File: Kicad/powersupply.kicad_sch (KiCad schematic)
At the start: 19 parts, among them J801 Jack 2/6.3mm, Q801 BC546, Q802 BC556, U801 DC-DC Module, U802 MAX1615, U803 TLV1117 3.3V 1A

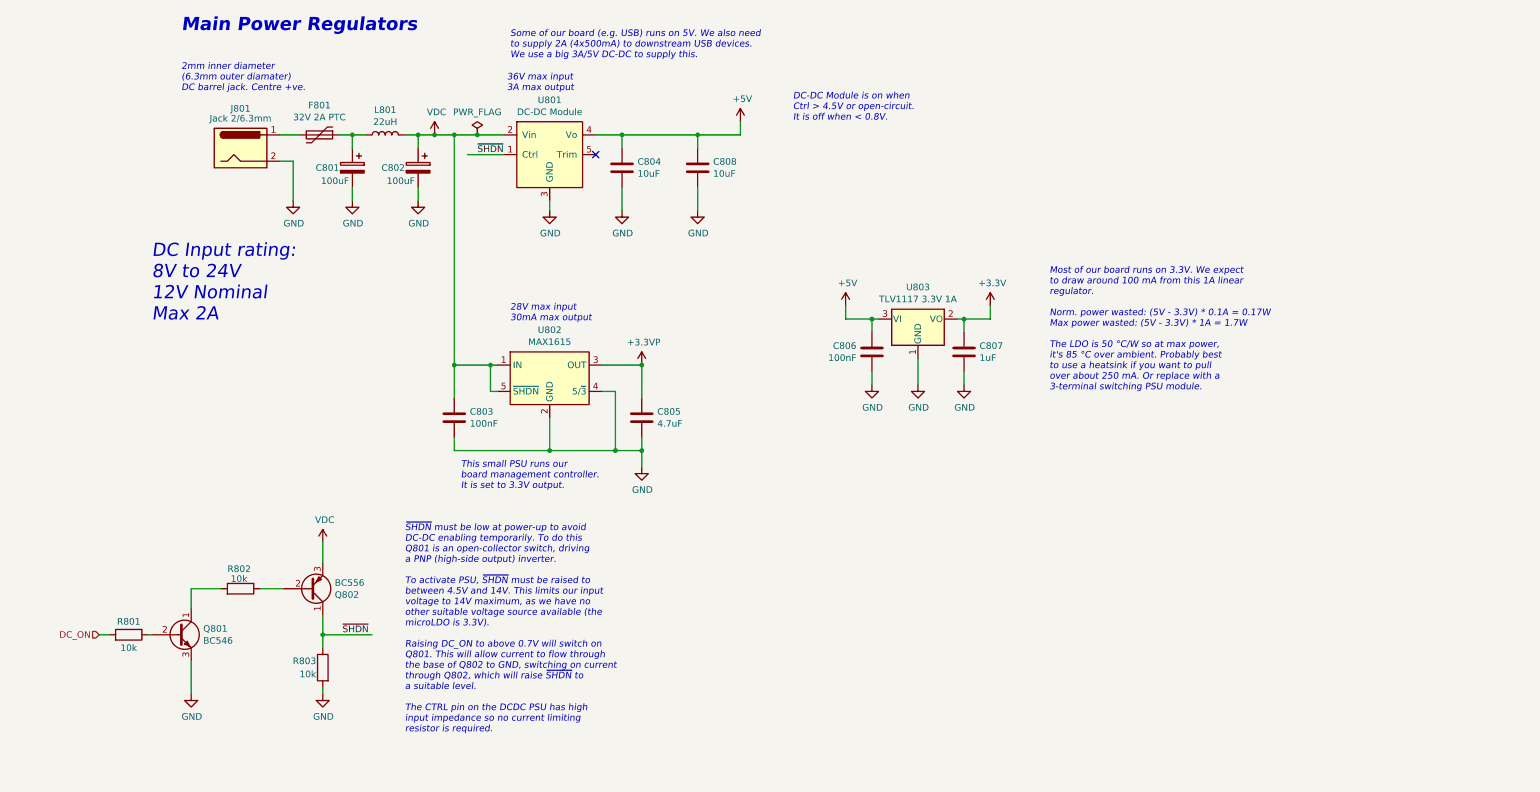
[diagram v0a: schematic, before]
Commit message: Retitle sheets and renumber parts.
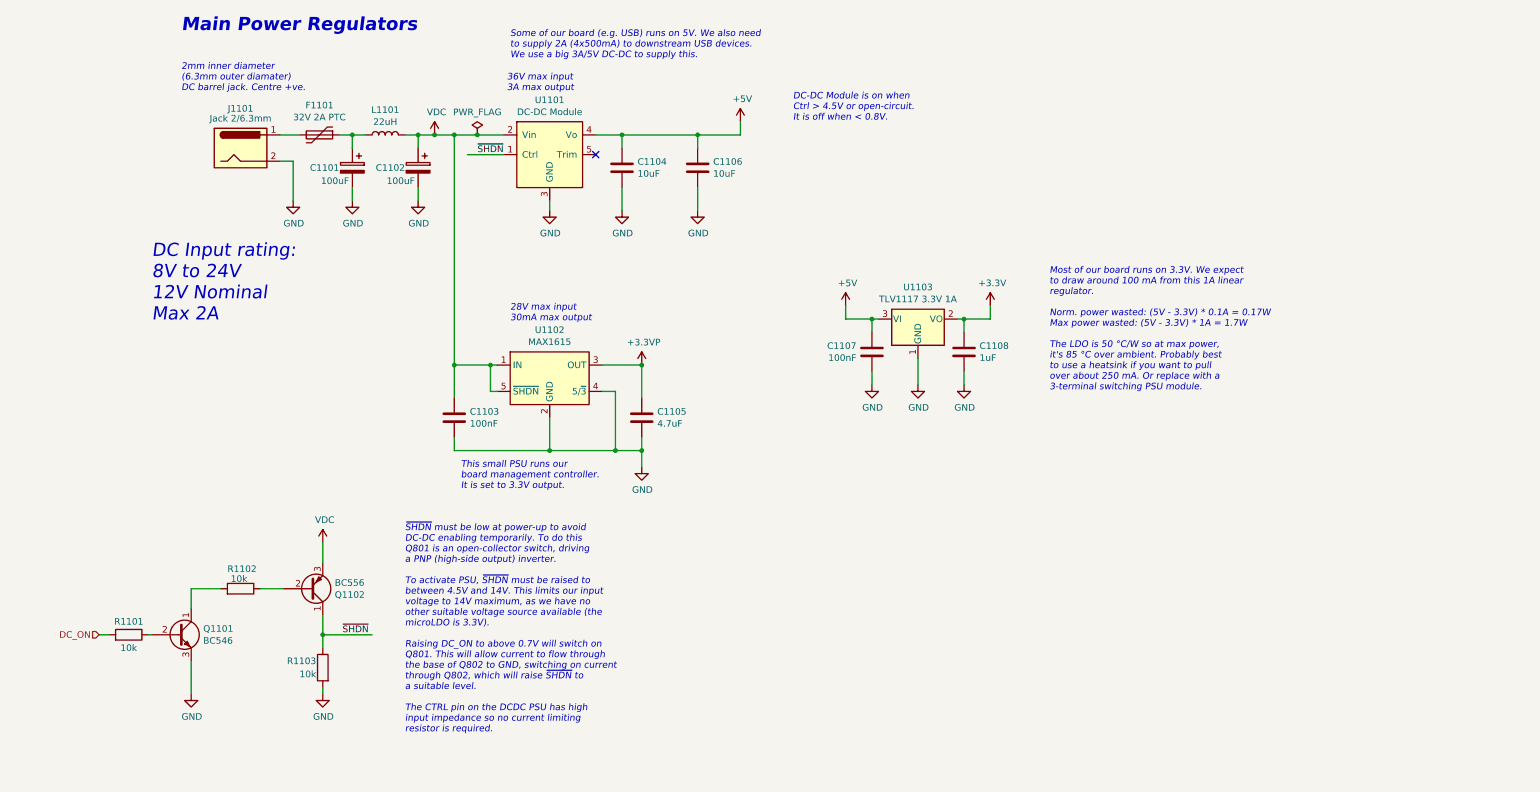
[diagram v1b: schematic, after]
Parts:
- renumbered C801 to C1101, C802 to C1102, C803 to C1103, C804 to C1104, C805 to C1105, C808 to C1106, C806 to C1107, C807 to C1108, F801 to F1101, J801 to J1101, L801 to L1101, Q801 to Q1101, Q802 to Q1102, R801 to R1101, R802 to R1102, R803 to R1103, U801 to U1101, U802 to U1102, U803 to U1103
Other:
- company: https://neotron-compute.github.io/ -> https://neotron-compute.github.io

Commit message: Power supply updates.
* Change out low-power standby LDO for HT7533
* Add P-FET reverse-polarity protection
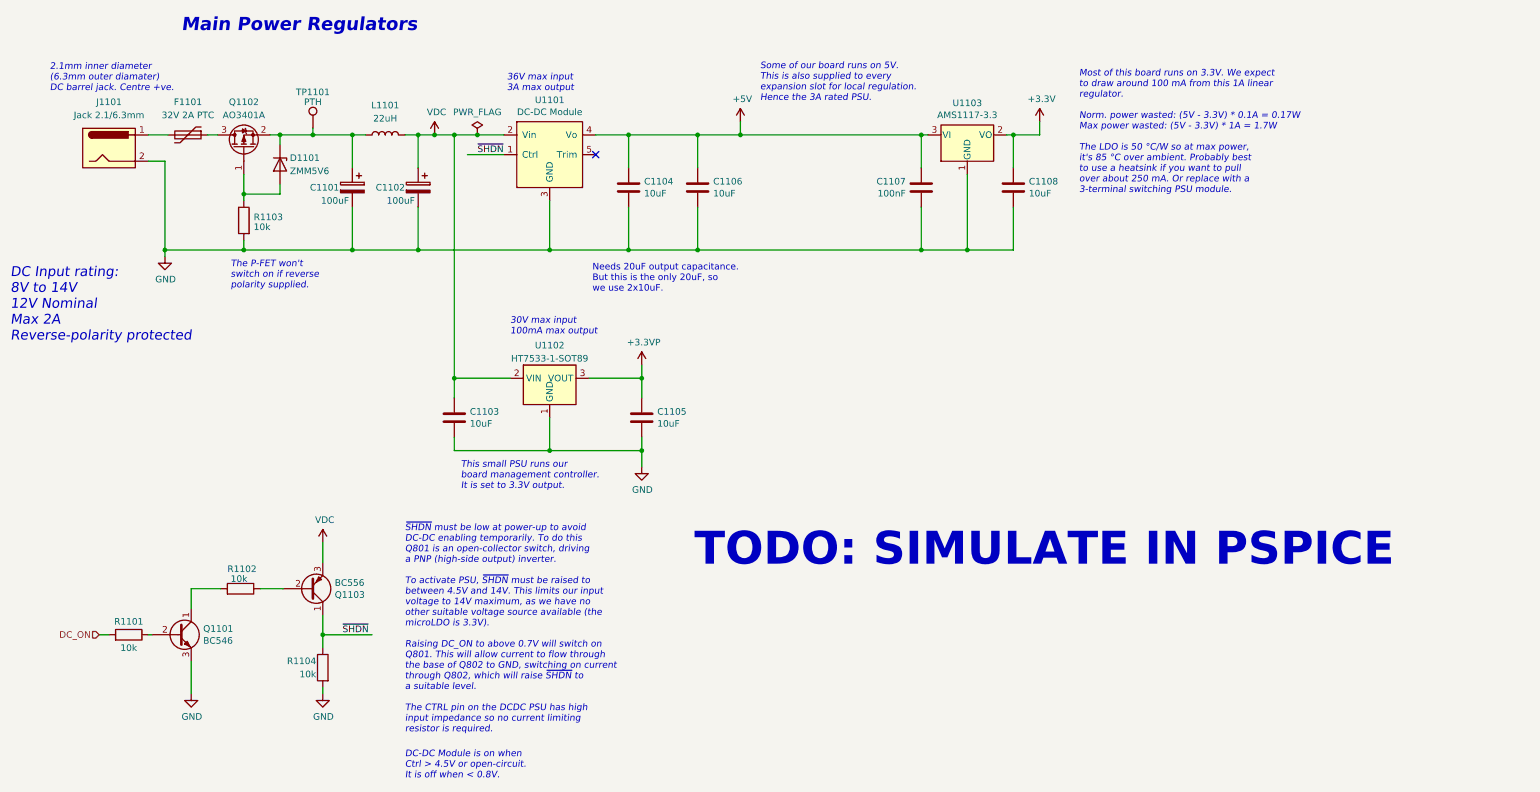
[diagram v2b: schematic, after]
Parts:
- removed U1102: MAX1615, Package_TO_SOT_SMD:SOT-23-5, symbol Regulator_Linear:MAX1615xUK
- added D1101: ZMM5V6, Diode_SMD:D_MiniMELF, symbol Diode:ZMMxx
- added Q1102: AO3401A, Package_TO_SOT_SMD:SOT-23, symbol Transistor_FET:AO3401A
- added R1103: 10k, Resistor_SMD:R_0805_2012Metric_Pad1.20x1.40mm_HandSolder, symbol Device:R
- added TP1101: PTH, TestPoint:TestPoint_THTPad_D1.5mm_Drill0.7mm, symbol Connector:TestPoint
- added U1102: HT7533-1-SOT89, Package_TO_SOT_SMD:SOT-89-3, symbol Regulator_Linear:HT75xx-1-SOT89
- C1103: value 100nF -> 10uF; LCSC Part# C49678 -> C15850; MPN CPL-CAP-X7R-0805-100NF-50V -> CPL-CAP-X5R-0805-10UF-16V; Voltage 50V -> 16V
- C1105: value 4.7uF -> 10uF; LCSC Part# C1779 -> C15850; MPN CPL-CAP-X5R-0805-4.7UF-25V -> CPL-CAP-X5R-0805-10UF-16V; Voltage 10V -> 16V
- C1108: value 1uF -> 10uF; LCSC Part# C28323 -> C15850; MPN CPL-CAP-X7R-0805-1UF-25V -> CPL-CAP-X5R-0805-10UF-16V; Voltage 10V -> 16V
- J1101: value Jack 2/6.3mm -> Jack 2.1/6.3mm
- U1103: value TLV1117 3.3V 1A -> AMS1117-3.3
- renumbered Q1102 to Q1103, R1103 to R1104
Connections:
- net +3.3VP: now also U1102.3 (VOUT)
- net GND: now also R1103.2, U1102.1 (GND)
- net VDC: now also U1102.2 (VIN)
- net at C1101.1, L1101.1: now also D1101.1 (K), Q1102.2 (S), TP1101.1; no longer F1101.1
- new net: F1101.1, Q1102.3 (D)
- new net: D1101.2 (A), Q1102.1 (G), R1103.1
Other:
- note added: "2.1mm inner diameter (6.3mm outer diamater) DC barrel jack. Centre +ve."
- note added: "30V max input 100mA max output"
- note added: "DC Input rating: 8V to 14V 12V Nominal Max 2A Reverse-polarity protected"
- note added: "Most of this board runs on 3.3V. We expect to draw around 100 mA from this 1A linear regulator. Norm. power wasted: (5V - 3.3V) * 0.1A = 0.17W Max power wasted: (5V - 3.3V) * 1A = 1.7W The LDO is 50 °C/W so at max power, it's 85 °C over ambient. Probably best to use a heatsink if you want to pull over about 250 mA. Or replace with a 3-terminal switching PSU module."
- note added: "Needs 20uF output capacitance. But this is the only 20uF, so we use 2x10uF."
- note added: "Some of our board runs on 5V. This is also supplied to every expansion slot for local regulation. Hence the 3A rated PSU."
- note added: "TODO: SIMULATE IN PSPICE"
- note added: "The P-FET won't switch on if reverse polarity supplied."
- note removed: "28V max input 30mA max output"
- note removed: "2mm inner diameter (6.3mm outer diamater) DC barrel jack. Centre +ve."
- note removed: "DC Input rating: 8V to 24V 12V Nominal Max 2A"
- note removed: "Most of our board runs on 3.3V. We expect to draw around 100 mA from this 1A linear regulator. Norm. power wasted: (5V - 3.3V) * 0.1A = 0.17W Max power wasted: (5V - 3.3V) * 1A = 1.7W The LDO is 50 °C/W so at max power, it's 85 °C over ambient. Probably best to use a heatsink if you want to pull over about 250 mA. Or replace with a 3-terminal switching PSU module."
- note removed: "Some of our board (e.g. USB) runs on 5V. We also need to supply 2A (4x500mA) to downstream USB devices. We use a big 3A/5V DC-DC to supply this."
- moved on the sheet: C1101, C1102, C1104, C1106, C1107, F1101, J1101, U1103

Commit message: Updated PCB with new footprints for PSU.
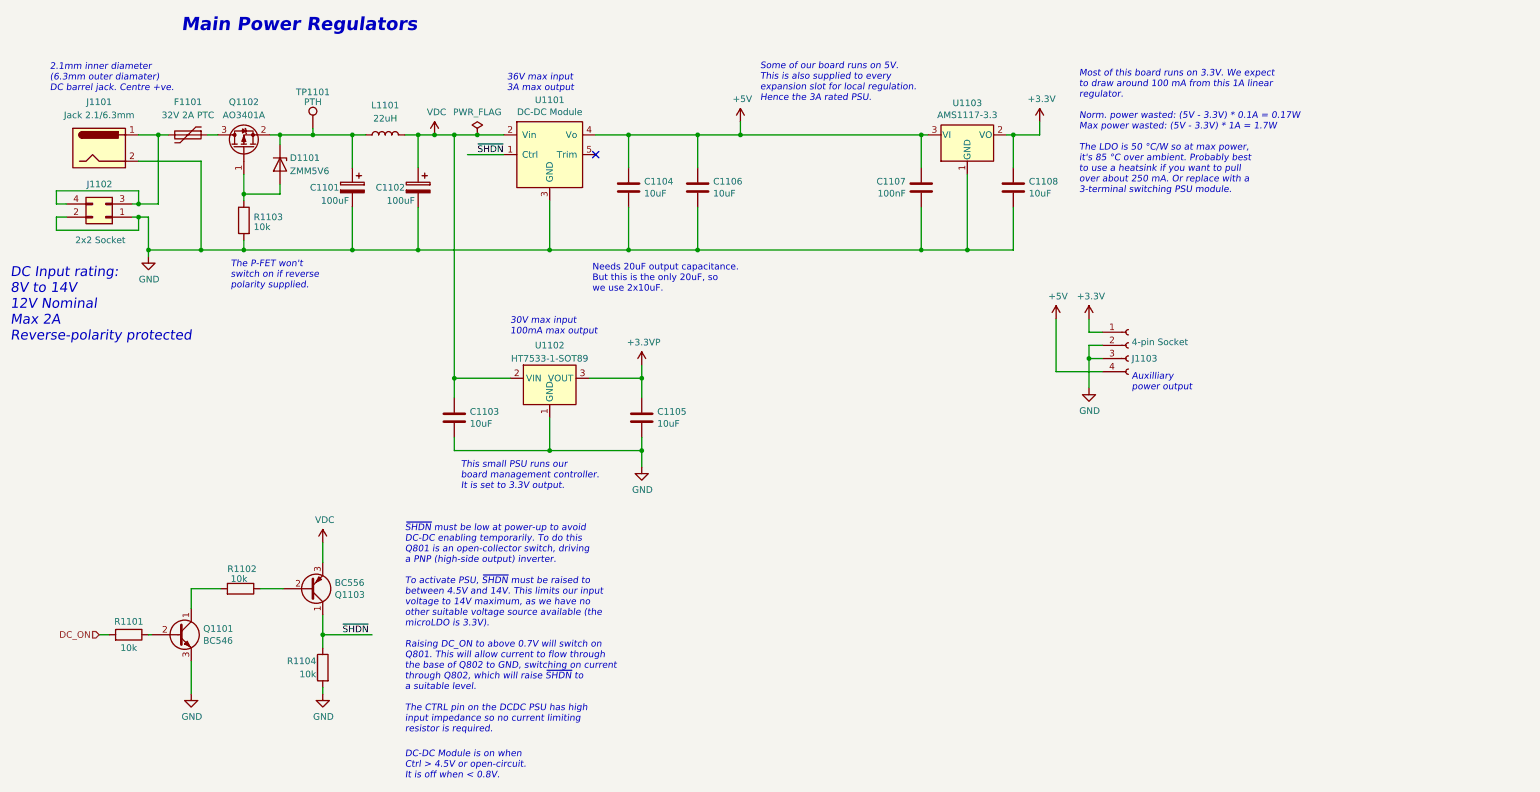
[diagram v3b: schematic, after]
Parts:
- added J1102: 2x2 Socket, Connector_PinSocket_2.54mm:PinSocket_2x02_P2.54mm_Vertical, symbol Connector_Generic:Conn_02x02_Odd_Even
- added J1103: 4-pin Socket, Connector_PinSocket_2.54mm:PinSocket_1x04_P2.54mm_Vertical, symbol Connector:Conn_01x04_Female
- F1101: footprint Fuse:Fuse_BelFuse_0ZRE0016FF_L9.9mm_W3.8mm -> neotron-pico:Bel Fuse 0ZRS0200FF
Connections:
- net +3V3: now also J1103.1 (Pin_1)
- net +5V: now also J1103.4 (Pin_4)
- net GND: now also J1102.1 (Pin_1), J1102.2 (Pin_2), J1103.2 (Pin_2), J1103.3 (Pin_3)
- net at F1101.2, J1101.1: now also J1102.3 (Pin_3), J1102.4 (Pin_4)
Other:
- note added: "Auxilliary power output"
- note removed: "TODO: SIMULATE IN PSPICE"
- moved on the sheet: J1101

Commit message: Set missing properties on components.
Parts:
- D1101: DNP (none) -> 0; Digikey (none) -> 1727-1888-2-ND; MPN (none) -> ZMM5V6; Manufacturer (none) -> Semtech; Voltage (none) -> 5.6V
- J1102, J1103, TP1101: DNP (none) -> 1
- Q1102: DNP (none) -> 0; Digikey (none) -> 785-1001-2-ND; MPN (none) -> AO3401A; Manufacturer (none) -> Alpha and Omega
- U1102: DNP (none) -> 0
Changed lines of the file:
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@@
   (symbol (lib_id "power:+3.3V") (at 214.63 51.435 0) (unit 1)
     (in_bom yes) (on_board yes)
-    (property "Reference" "#PWR01113" (id 0) (at 214.63 55.245 0)
+    (property "Reference" "#PWR01109" (id 0) (at 214.63 55.245 0)
       (effects (font (size 1.27 1.27)) hide)
     )
@@
       (effects (font (size 1.27 1.27)) hide)
     )
+    (property "DNP" "1" (id 4) (at 231.775 94.615 0)
+      (effects (font (size 1.27 1.27)) hide)
+    )
+    (property "Digikey" "~" (id 5) (at 231.775 94.615 0)
+      (effects (font (size 1.27 1.27)) hide)
+    )
+    (property "LCSC Part#" "~" (id 6) (at 231.775 94.615 0)
+      (effects (font (size 1.27 1.27)) hide)
+    )
+    (property "MPN" "~" (id 7) (at 231.775 94.615 0)
+      (effects (font (size 1.27 1.27)) hide)
+    )
+    (property "Manufacturer" "~" (id 8) (at 231.775 94.615 0)
+      (effects (font (size 1.27 1.27)) hide)
+    )
+    (property "Mouser" "~" (id 9) (at 231.775 94.615 0)
+      (effects (font (size 1.27 1.27)) hide)
+    )
+    (property "Tolerance" "~" (id 10) (at 231.775 94.615 0)
+      (effects (font (size 1.27 1.27)) hide)
+    )
+    (property "Voltage" "~" (id 11) (at 231.775 94.615 0)
+      (effects (font (size 1.27 1.27)) hide)
+    )
     (pin "1")
     (pin "2")
@@
   (symbol (lib_id "power:GND") (at 224.155 102.87 0) (unit 1)
     (in_bom yes) (on_board yes)
-    (property "Reference" "#PWR01111" (id 0) (at 224.155 109.22 0)
+    (property "Reference" "#PWR01112" (id 0) (at 224.155 109.22 0)
       (effects (font (size 1.27 1.27)) hide)
     )
@@
   (symbol (lib_id "power:+5V") (at 217.805 89.535 0) (unit 1)
     (in_bom yes) (on_board yes)
-    (property "Reference" "#PWR01109" (id 0) (at 217.805 93.345 0)
+    (property "Reference" "#PWR01110" (id 0) (at 217.805 93.345 0)
       (effects (font (size 1.27 1.27)) hide)
     )
@@
       (effects (font (size 1.27 1.27)) hide)
     )
+    (property "DNP" "1" (id 4) (at 34.29 69.85 0)
+      (effects (font (size 1.27 1.27)) hide)
+    )
+    (property "Digikey" "~" (id 5) (at 34.29 69.85 0)
+      (effects (font (size 1.27 1.27)) hide)
+    )
+    (property "LCSC Part#" "~" (id 6) (at 34.29 69.85 0)
+      (effects (font (size 1.27 1.27)) hide)
+    )
+    (property "MPN" "~" (id 7) (at 34.29 69.85 0)
+      (effects (font (size 1.27 1.27)) hide)
+    )
+    (property "Manufacturer" "~" (id 8) (at 34.29 69.85 0)
+      (effects (font (size 1.27 1.27)) hide)
+    )
+    (property "Mouser" "~" (id 9) (at 34.29 69.85 0)
+      (effects (font (size 1.27 1.27)) hide)
+    )
+    (property "Tolerance" "~" (id 10) (at 34.29 69.85 0)
+      (effects (font (size 1.27 1.27)) hide)
+    )
+    (property "Voltage" "~" (id 11) (at 34.29 69.85 0)
+      (effects (font (size 1.27 1.27)) hide)
+    )
     (pin "1")
     (pin "2")
@@
       (effects (font (size 1.27 1.27)) hide)
     )
+    (property "DNP" "0" (id 5) (at 67.945 59.69 0)
+      (effects (font (size 1.27 1.27)) hide)
+    )
+    (property "Digikey" "1727-1888-2-ND" (id 6) (at 67.945 59.69 0)
+      (effects (font (size 1.27 1.27)) hide)
+    )
+    (property "MPN" "ZMM5V6" (id 7) (at 67.945 59.69 0)
+      (effects (font (size 1.27 1.27)) hide)
+    )
+    (property "Manufacturer" "Semtech" (id 8) (at 67.945 59.69 0)
+      (effects (font (size 1.27 1.27)) hide)
+    )
+    (property "Mouser" "~" (id 9) (at 67.945 59.69 0)
+      (effects (font (size 1.27 1.27)) hide)
+    )
+    (property "Tolerance" "~" (id 10) (at 67.945 59.69 0)
+      (effects (font (size 1.27 1.27)) hide)
+    )
+    (property "Voltage" "5.6V" (id 11) (at 67.945 59.69 0)
+      (effects (font (size 1.27 1.27)) hide)
+    )
     (pin "1")
     (pin "2")
@@
   (symbol (lib_id "power:+3.3V") (at 224.155 89.535 0) (unit 1)
     (in_bom yes) (on_board yes)
-    (property "Reference" "#PWR01110" (id 0) (at 224.155 93.345 0)
+    (property "Reference" "#PWR01111" (id 0) (at 224.155 93.345 0)
       (effects (font (size 1.27 1.27)) hide)
     )
@@
       (effects (font (size 1.27 1.27)) hide)
     )
+    (property "DNP" "0" (id 5) (at 120.015 103.505 0)
+      (effects (font (size 1.27 1.27)) hide)
+    )
+    (property "Digikey" "~" (id 6) (at 120.015 103.505 0)
+      (effects (font (size 1.27 1.27)) hide)
+    )
+    (property "MPN" "~" (id 7) (at 120.015 103.505 0)
+      (effects (font (size 1.27 1.27)) hide)
+    )
+    (property "Manufacturer" "~" (id 8) (at 120.015 103.505 0)
+      (effects (font (size 1.27 1.27)) hide)
+    )
+    (property "Mouser" "~" (id 9) (at 120.015 103.505 0)
+      (effects (font (size 1.27 1.27)) hide)
+    )
+    (property "Tolerance" "~" (id 10) (at 120.015 103.505 0)
+      (effects (font (size 1.27 1.27)) hide)
+    )
+    (property "Voltage" "~" (id 11) (at 120.015 103.505 0)
+      (effects (font (size 1.27 1.27)) hide)
+    )
     (pin "1")
     (pin "2")
@@
     )
     (property "Datasheet" "~" (id 3) (at 79.375 52.705 0)
+      (effects (font (size 1.27 1.27)) hide)
+    )
+    (property "DNP" "1" (id 4) (at 74.295 52.705 0)
+      (effects (font (size 1.27 1.27)) hide)
+    )
+    (property "Digikey" "~" (id 5) (at 74.295 52.705 0)
+      (effects (font (size 1.27 1.27)) hide)
+    )
+    (property "LCSC Part#" "~" (id 6) (at 74.295 52.705 0)
+      (effects (font (size 1.27 1.27)) hide)
+    )
+    (property "MPN" "~" (id 7) (at 74.295 52.705 0)
+      (effects (font (size 1.27 1.27)) hide)
+    )
+    (property "Manufacturer" "~" (id 8) (at 74.295 52.705 0)
+      (effects (font (size 1.27 1.27)) hide)
+    )
+    (property "Mouser" "~" (id 9) (at 74.295 52.705 0)
+      (effects (font (size 1.27 1.27)) hide)
+    )
+    (property "Tolerance" "~" (id 10) (at 74.295 52.705 0)
+      (effects (font (size 1.27 1.27)) hide)
+    )
+    (property "Voltage" "~" (id 11) (at 74.295 52.705 0)
       (effects (font (size 1.27 1.27)) hide)
     )
@@
       (effects (font (size 1.27 1.27)) hide)
     )
+    (property "DNP" "0" (id 5) (at 60.96 56.515 0)
+      (effects (font (size 1.27 1.27)) hide)
+    )
+    (property "Digikey" "785-1001-2-ND" (id 6) (at 60.96 56.515 0)
+      (effects (font (size 1.27 1.27)) hide)
+    )
+    (property "MPN" "AO3401A" (id 7) (at 60.96 56.515 0)
+      (effects (font (size 1.27 1.27)) hide)
+    )
+    (property "Manufacturer" "Alpha and Omega" (id 8) (at 60.96 56.515 0)
+      (effects (font (size 1.27 1.27)) hide)
+    )
+    (property "Mouser" "~" (id 9) (at 60.96 56.515 0)
+      (effects (font (size 1.27 1.27)) hide)
+    )
+    (property "Tolerance" "~" (id 10) (at 60.96 56.515 0)
+      (effects (font (size 1.27 1.27)) hide)
+    )
+    (property "Voltage" "~" (id 11) (at 60.96 56.515 0)
+      (effects (font (size 1.27 1.27)) hide)
+    )
